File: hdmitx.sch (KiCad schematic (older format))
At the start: 56 parts, among them J4 HDMI_CONN, U15 TLV70018, U16 TLV70018, U3 IT6613, U8 PCM1862, Y2 24.576MHz

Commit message: add test pins fix tracks
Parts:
- added J21: I2C_BCK, custom_components:TestPad-D1.0mm, symbol Connector_Generic:Conn_01x01
- added J22: I2C_WS, custom_components:TestPad-D1.0mm, symbol Connector_Generic:Conn_01x01
- added J23: I2C_DATA, custom_components:TestPad-D1.0mm, symbol Connector_Generic:Conn_01x01
- added J24: I2C_MCLK, custom_components:TestPad-D1.0mm, symbol Connector_Generic:Conn_01x01
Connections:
- wire segments 132 -> 176
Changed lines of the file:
@@
 EESchema Schematic File Version 4
 LIBS:ossc_board-cache
-EELAYER 26 0
+EELAYER 30 0
 EELAYER END
 $Descr A4 11693 8268
@@
 $EndComp
 $Comp
-L ossc_board-rescue:GND-RESCUE-ossc_board #PWR0170
-U 1 1 5501F4D5
-P 2250 3000
-F 0 "#PWR0170" H 2250 3000 30  0001 C CNN
-F 1 "GND" H 2250 2930 30  0001 C CNN
-F 2 "" H 2250 3000 60  0001 C CNN
-F 3 "" H 2250 3000 60  0000 C CNN
-	1    2250 3000
-	0    1    1    0
-$EndComp
-$Comp
 L ossc_board-rescue:GND-RESCUE-ossc_board #PWR0171
 U 1 1 5501F4DB
@@
 AVCC1V8
 Wire Wire Line
-	3250 5500 3250 6500
+	3250 5500 3250 6450
 Wire Wire Line
 	3250 7200 3250 7650
@@
 	3000 7200 3000 6450
 Wire Wire Line
-	3000 6450 3250 6450
-Wire Wire Line
-	4650 5500 4650 6500
+	3000 6450 3100 6450
+Wire Wire Line
+	4650 5500 4650 6450
 Wire Wire Line
 	4650 7200 4650 7650
@@
 	4400 7200 4400 6450
 Wire Wire Line
-	4400 6450 4650 6450
-Wire Wire Line
-	3650 5500 3650 6500
+	4400 6450 4500 6450
+Wire Wire Line
+	3650 5500 3650 6450
 Wire Wire Line
 	3650 7200 3650 7650
@@
 	3400 7200 3400 6450
 Wire Wire Line
-	3400 6450 4250 6450
+	3400 6450 3500 6450
 Wire Wire Line
 	2700 6000 3150 6000
@@
 	6250 3700 6750 3700
 Wire Wire Line
-	5450 1900 5450 2100
-Wire Wire Line
-	3150 1900 3150 2100
-Wire Wire Line
 	1800 3700 2250 3700
 Wire Wire Line
@@
 	7500 5000 6250 5000
 Wire Wire Line
-	8500 2900 9450 2900
-Wire Wire Line
-	8500 3000 9450 3000
-Wire Wire Line
-	8500 3200 9450 3200
-Wire Wire Line
-	8500 3300 9450 3300
-Wire Wire Line
-	8500 3500 9450 3500
-Wire Wire Line
-	8500 3600 9450 3600
-Wire Wire Line
-	8500 3800 9450 3800
-Wire Wire Line
-	8500 3900 9450 3900
+	8500 2900 9100 2900
+Wire Wire Line
+	8500 3000 9100 3000
+Wire Wire Line
+	8500 3200 9100 3200
+Wire Wire Line
+	8500 3300 9100 3300
+Wire Wire Line
+	8500 3500 9100 3500
+Wire Wire Line
+	8500 3600 9100 3600
+Wire Wire Line
+	8500 3800 9100 3800
+Wire Wire Line
+	8500 3900 9100 3900
 Wire Wire Line
 	8050 6450 7600 6450
@@
 	9950 5900 9950 5950
 Wire Wire Line
-	9350 5950 10500 5950
-Wire Wire Line
-	10400 5550 10700 5550
+	9350 5950 9950 5950
+Wire Wire Line
+	10400 5550 10500 5550
 Wire Wire Line
 	9500 5550 9500 5700
@@
 	9950 6850 9950 6900
 Wire Wire Line
-	9350 6900 10500 6900
-Wire Wire Line
-	8750 6500 9500 6500
-Wire Wire Line
-	10400 6500 10700 6500
+	9350 6900 9950 6900
+Wire Wire Line
+	8750 6500 9350 6500
+Wire Wire Line
+	10400 6500 10500 6500
 Wire Wire Line
 	9500 6500 9500 6650
@@
 Wire Notes Line
 	10100 4600 10100 4500
-Wire Wire Line
-	3150 1600 3150 2000
-Connection ~ 3150 2000
-Wire Wire Line
-	5450 1950 5450 1600
-Connection ~ 5450 1950
 $Comp
 L ossc_board-rescue:FILTER FB4
@@
 Connection ~ 4000 6450
 Wire Wire Line
-	8750 5550 9500 5550
+	8750 5550 9350 5550
 Text Label 8850 5550 0    60   ~ 0
 DVDD3V3
@@
 DVDD1V8
 Wire Wire Line
-	8950 4650 9550 4650
+	8950 4650 9250 4650
 $Comp
 L ossc_board-rescue:R R41
@@
 DDC_SCL
 Wire Wire Line
-	8300 4250 9550 4250
-Wire Wire Line
-	7650 4350 9550 4350
+	8300 4250 8750 4250
+Wire Wire Line
+	7650 4350 8150 4350
 Text Label 7650 4350 0    60   ~ 0
 DDC_SDA
@@
 Connection ~ 8750 4250
 Wire Wire Line
-	8300 4550 9550 4550
+	8300 4550 8750 4550
 $Comp
 L ossc_board-rescue:PWR_FLAG #FLG0226
@@
 $EndComp
 Wire Wire Line
-	7700 2200 8250 2200
+	7700 2200 7900 2200
 Connection ~ 7900 2200
 $Comp
@@
 $EndComp
 Wire Wire Line
-	7250 1600 8250 1600
+	7250 1600 7450 1600
 Text Label 7300 1600 0    60   ~ 0
 AVCC3V3
@@
 	7650 1700 7650 1950
 Wire Wire Line
-	7650 1950 6900 1950
+	7650 1950 7100 1950
 Wire Wire Line
 	8250 1800 7750 1800
@@
 Wire Wire Line
 	2250 3400 1700 3400
-Wire Wire Line
-	2250 3500 1700 3500
-Wire Wire Line
-	2250 3600 1700 3600
 Text Label 1750 3400 0    60   ~ 0
 I2S_DATA
@@
 AV3_AUD_R
 Wire Wire Line
-	10050 900  10650 900
-Wire Wire Line
-	10050 1100 10650 1100
-Wire Wire Line
-	7250 900  8050 900
+	10050 900  10550 900
+Wire Wire Line
+	10050 1100 10450 1100
+Wire Wire Line
+	7250 900  7400 900
 Wire Wire Line
 	8750 4250 8750 4100
@@
 $EndComp
 Wire Wire Line
-	8500 3100 9400 3100
+	8500 3100 9100 3100
 Connection ~ 9100 3100
 Connection ~ 9400 3000
@@
 $EndComp
 Wire Wire Line
-	8500 3700 9400 3700
+	8500 3700 9100 3700
 Connection ~ 9100 3700
 Connection ~ 9400 3800
@@
 Connection ~ 7400 900
 Wire Wire Line
-	7250 1000 7800 1000
+	7250 1000 7400 1000
 Connection ~ 7400 1000
 $Comp
@@
 $EndComp
 Wire Wire Line
-	10200 1200 10650 1200
+	10200 1200 10550 1200
 $Comp
 L ossc_board-rescue:GND #PWR0246
@@
 $EndComp
 Wire Wire Line
-	10650 1000 10200 1000
+	10650 1000 10450 1000
 Wire Wire Line
 	10450 850  10450 1000
@@
 NoConn ~ 8250 1100
 NoConn ~ 8250 1200
+Wire Wire Line
+	3250 6450 3250 6500
+Wire Wire Line
+	4650 6450 4650 6500
+Wire Wire Line
+	3650 6450 3650 6500
+Wire Wire Line
+	3650 6450 4000 6450
+Wire Wire Line
+	9350 5550 9500 5550
+Wire Wire Line
+	10500 5550 10700 5550
+Wire Wire Line
+	9950 5950 10500 5950
+Wire Wire Line
+	9350 6500 9500 6500
+Wire Wire Line
+	10500 6500 10700 6500
+Wire Wire Line
+	9950 6900 10500 6900
+Wire Wire Line
+	3100 6450 3250 6450
+Wire Wire Line
+	3500 6450 3650 6450
+Wire Wire Line
+	4500 6450 4650 6450
+Wire Wire Line
+	4000 6450 4250 6450
+Wire Wire Line
+	9250 4650 9550 4650
+Wire Wire Line
+	8150 4350 9550 4350
+Wire Wire Line
+	8750 4250 9550 4250
+Wire Wire Line
+	8750 4550 9550 4550
+Wire Wire Line
+	7900 2200 8250 2200
+Wire Wire Line
+	7450 1600 8250 1600
+Wire Wire Line
+	7100 1950 6900 1950
+Wire Wire Line
+	9100 3100 9400 3100
+Wire Wire Line
+	9400 3000 9450 3000
+Wire Wire Line
+	9100 3000 9400 3000
+Wire Wire Line
+	9400 2900 9450 2900
+Wire Wire Line
+	9100 2900 9400 2900
+Wire Wire Line
+	9400 3200 9450 3200
+Wire Wire Line
+	9100 3200 9400 3200
+Wire Wire Line
+	9400 3300 9450 3300
+Wire Wire Line
+	9100 3300 9400 3300
+Wire Wire Line
+	9400 3500 9450 3500
+Wire Wire Line
+	9100 3500 9400 3500
+Wire Wire Line
+	9400 3600 9450 3600
+Wire Wire Line
+	9100 3600 9400 3600
+Wire Wire Line
+	9100 3700 9400 3700
+Wire Wire Line
+	9400 3800 9450 3800
+Wire Wire Line
+	9100 3800 9400 3800
+Wire Wire Line
+	9400 3900 9450 3900
+Wire Wire Line
+	9100 3900 9400 3900
+Wire Wire Line
+	7400 900  8050 900
+Wire Wire Line
+	7400 1000 7800 1000
+Wire Wire Line
+	10450 1000 10200 1000
+Wire Wire Line
+	10550 900  10650 900
+Wire Wire Line
+	10450 1100 10650 1100
+Wire Wire Line
+	10550 1200 10650 1200
+Wire Wire Line
+	3150 1600 3150 2100
+Wire Wire Line
+	5450 1600 5450 2100
+$Comp
+L Connector_Generic:Conn_01x01 J21
+U 1 1 5ED4EADB
+P 1200 3600
+F 0 "J21" H 1118 3375 50  0000 C CNN
+F 1 "I2C_BCK" H 1118 3466 50  0000 C CNN
+F 2 "custom_components:TestPad-D1.0mm" H 1200 3600 50  0001 C CNN
+F 3 "~" H 1200 3600 50  0001 C CNN
+	1    1200 3600
+	-1   0    0    1
+$EndComp
+$Comp
+L Connector_Generic:Conn_01x01 J22
+U 1 1 5ED547BE
+P 1350 3500
+F 0 "J22" H 1268 3275 50  0000 C CNN
+F 1 "I2C_WS" H 1268 3366 50  0000 C CNN
+F 2 "custom_components:TestPad-D1.0mm" H 1350 3500 50  0001 C CNN
+F 3 "~" H 1350 3500 50  0001 C CNN
+	1    1350 3500
+	-1   0    0    1
+$EndComp
+$Comp
+L Connector_Generic:Conn_01x01 J23
+U 1 1 5ED55109
+P 1500 3400
+F 0 "J23" H 1418 3175 50  0000 C CNN
+F 1 "I2C_DATA" H 1418 3266 50  0000 C CNN
+F 2 "custom_components:TestPad-D1.0mm" H 1500 3400 50  0001 C CNN
+F 3 "~" H 1500 3400 50  0001 C CNN
+	1    1500 3400
+	-1   0    0    1
+$EndComp
+Wire Wire Line
+	1550 3500 2250 3500
+Wire Wire Line
+	1400 3600 2250 3600
+$Comp
+L Connector_Generic:Conn_01x01 J24
+U 1 1 5ED68957
+P 1550 3000
+F 0 "J24" H 1468 2775 50  0000 C CNN
+F 1 "I2C_MCLK" H 1468 2866 50  0000 C CNN
+F 2 "custom_components:TestPad-D1.0mm" H 1550 3000 50  0001 C CNN
+F 3 "~" H 1550 3000 50  0001 C CNN
+	1    1550 3000
+	-1   0    0    1
+$EndComp
+Wire Wire Line
+	1750 3000 2250 3000
 $EndSCHEMATC

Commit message: remove unnecessary component
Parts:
- removed C111, C112: 30p, custom_components:SM0603_Capa_libcms, symbol ossc_board-rescue:C_Small
- removed C113, C115, C116, C121, C123, C124, C125, C126: 10u, custom_components:SM0603_Capa_libcms, symbol ossc_board-rescue:C_Small
- removed C114, C118: 0.1u, custom_components:SM0603_Capa_libcms, symbol ossc_board-rescue:C_Small
- removed C119, C120: 2.2u, custom_components:SM0603_Capa_libcms, symbol ossc_board-rescue:C_Small
- removed R47, R48, R49, R50, R51, R52: 100k, custom_components:SM0603_Resistor_libcms, symbol ossc_board-rescue:R_Small
- removed U8: PCM1862, custom_components:TSSOP-30_4.4x7.8mm_Pitch0.5mm_Handsoldering, symbol ossc_board-rescue:PCM1862
- removed Y2: 24.576MHz, custom_components:ECS-3X9X, symbol ossc_board-rescue:Crystal_Small
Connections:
- net labels removed: AV1_AUD_L, AV1_AUD_R, AV2_AUD_L, AV2_AUD_R, AV3_AUD_L, AV3_AUD_R
- wire segments 176 -> 129
- no-connect marks 10 -> 3

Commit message: update PCB
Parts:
- removed J21: I2C_BCK, custom_components:TestPad-D1.0mm, symbol Connector_Generic:Conn_01x01
- removed J22: I2C_WS, custom_components:TestPad-D1.0mm, symbol Connector_Generic:Conn_01x01
- removed J23: I2C_DATA, custom_components:TestPad-D1.0mm, symbol Connector_Generic:Conn_01x01
- removed J24: I2C_MCLK, custom_components:TestPad-D1.0mm, symbol Connector_Generic:Conn_01x01
- C110, C69, C73, C74, C75, C77, C78, C79, C80, C81, C82, C83, C84, C85, C86, C87, C88, C89, C90: footprint custom_components:SM0603_Capa_libcms -> Capacitor_SMD:C_0603_1608Metric_Pad1.05x0.95mm_HandSolder
- F1: renamed from F2; footprint custom_components:SM0603_Resistor_libcms -> Inductor_SMD:L_0603_1608Metric_Pad1.05x0.95mm_HandSolder
- FB1, FB2, FB4: footprint custom_components:SM0603_Resistor_libcms -> Inductor_SMD:L_0603_1608Metric_Pad1.05x0.95mm_HandSolder
- R25, R26, R41, R45, R46: footprint custom_components:SM0603_Resistor_libcms -> Resistor_SMD:R_0603_1608Metric_Pad1.05x0.95mm_HandSolder
- renumbered J4 to J1
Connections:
- net labels added: I2S_LRCK, I2S_MCLK
- net labels removed: I2S_WS

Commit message: update3
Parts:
- R25: value 698 -> 698 1%
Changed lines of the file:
@@
 P 3150 5750
 F 0 "R25" V 3230 5750 40  0000 C CNN
-F 1 "698" V 3157 5751 40  0000 C CNN
+F 1 "698 1%" V 3157 5751 40  0000 C CNN
 F 2 "Resistor_SMD:R_0603_1608Metric_Pad1.05x0.95mm_HandSolder" V 3080 5750 30  0001 C CNN
 F 3 "~" H 3150 5750 30  0000 C CNN

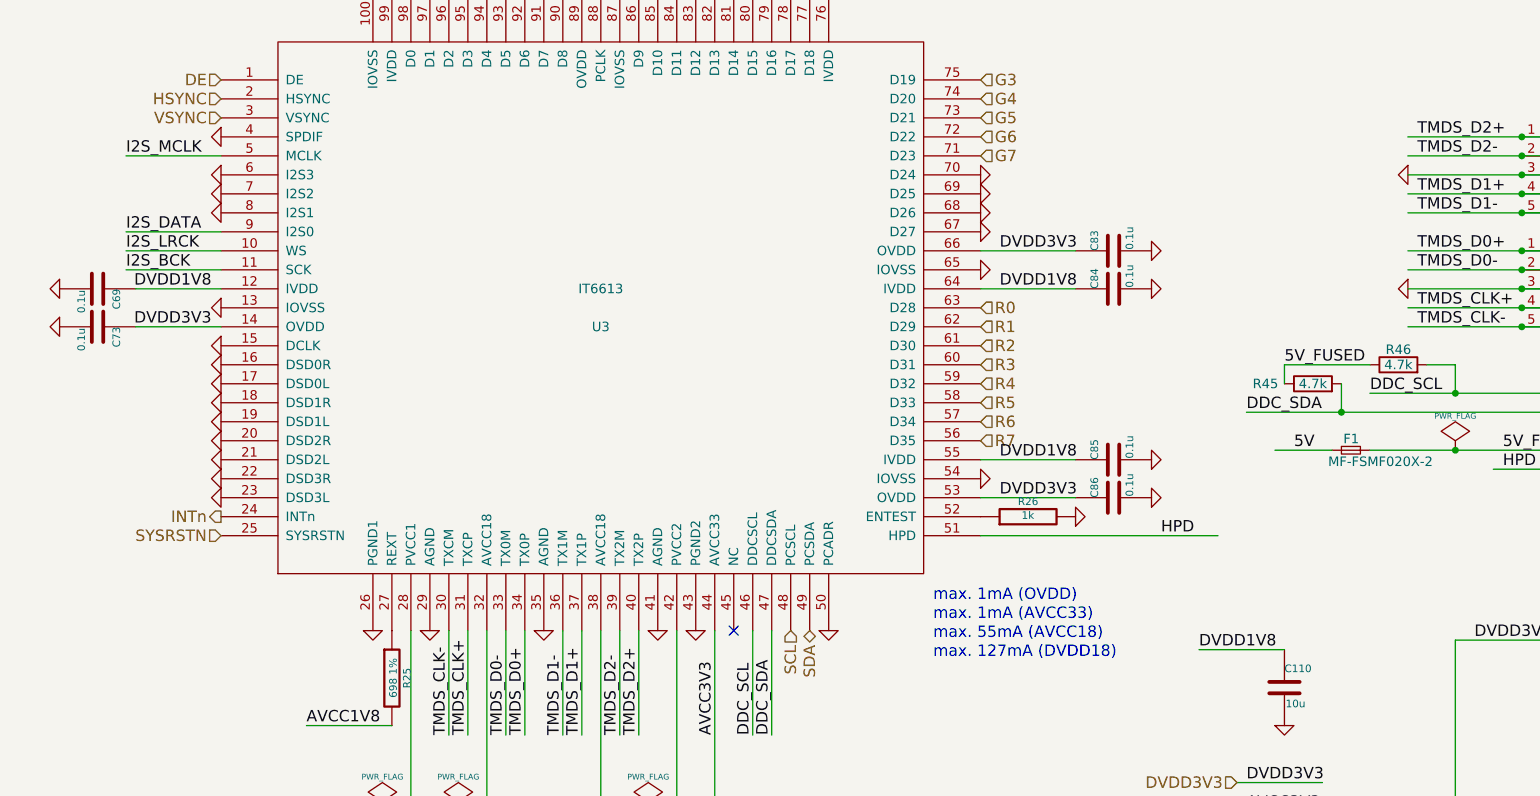
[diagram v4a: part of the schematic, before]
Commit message: add adc
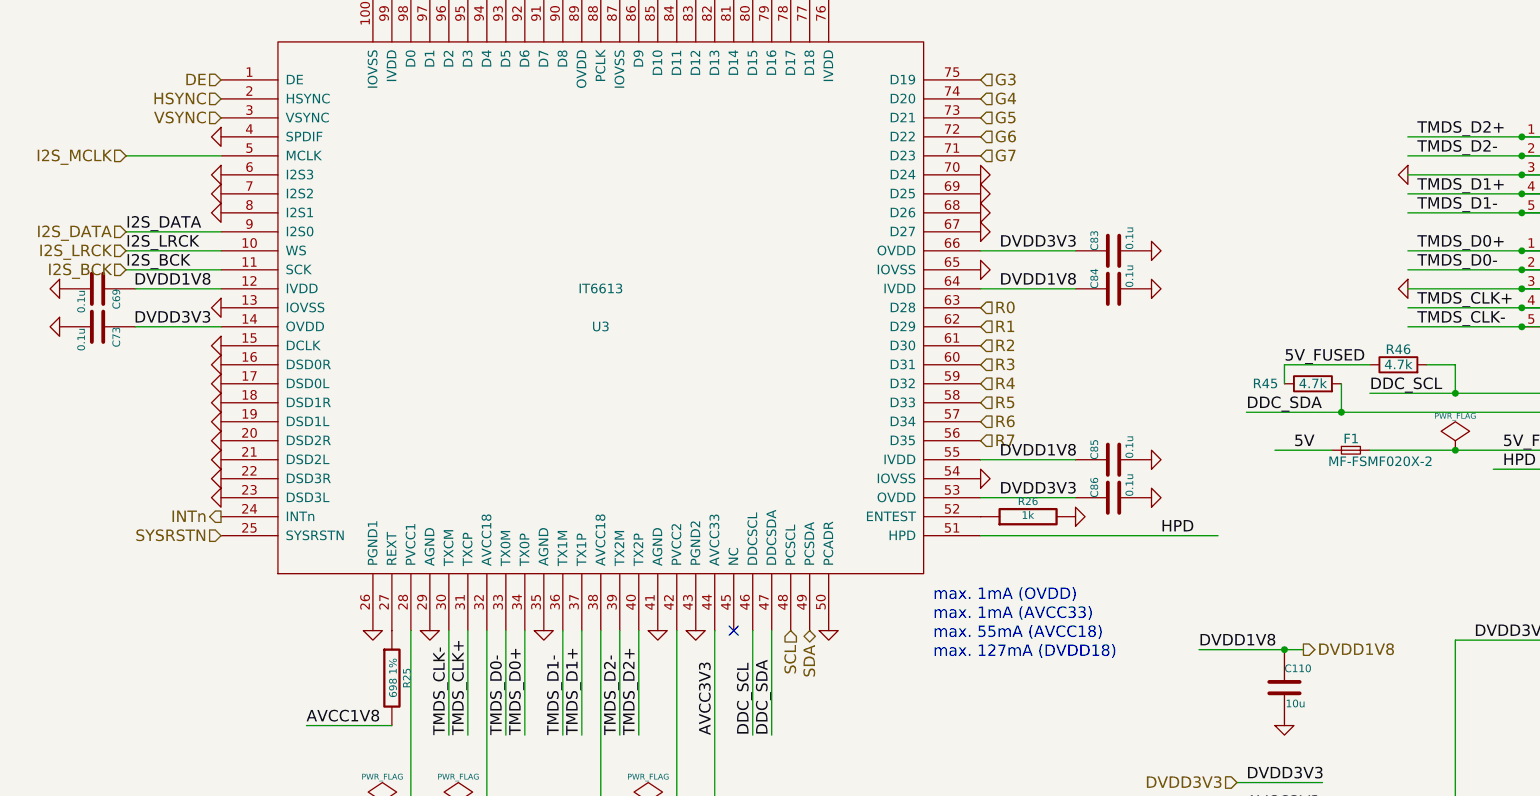
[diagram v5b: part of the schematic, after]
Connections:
- wire segments 129 -> 130
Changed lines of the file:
@@
 Text Label 7850 4100 0    60   ~ 0
 5V_FUSED
-Text Label 1750 3400 0    60   ~ 0
-I2S_DATA
 Text Label 1750 3600 0    60   ~ 0
 I2S_BCK
@@
 Wire Wire Line
 	1750 3000 2250 3000
-Text Label 1750 3000 0    60   ~ 0
+Wire Wire Line
+	2250 3600 1750 3600
+Wire Wire Line
+	1750 3500 2250 3500
+Wire Wire Line
+	2250 3400 1750 3400
+Text HLabel 7950 5600 2    60   Output ~ 0
+DVDD1V8
+Wire Wire Line
+	7950 5600 7850 5600
+Connection ~ 7850 5600
+Text HLabel 1750 3000 0    60   Input ~ 0
 I2S_MCLK
-Wire Wire Line
-	2250 3600 1750 3600
-Wire Wire Line
-	1750 3500 2250 3500
-Wire Wire Line
-	2250 3400 1750 3400
+Text Label 1750 3400 0    60   ~ 0
+I2S_DATA
+Text HLabel 1750 3400 0    60   Input ~ 0
+I2S_DATA
+Text HLabel 1750 3500 0    60   Input ~ 0
+I2S_LRCK
+Text HLabel 1750 3600 0    60   Input ~ 0
+I2S_BCK
 $EndSCHEMATC

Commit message: update PCB
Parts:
- J1: value HDMI_CONN -> HDMI_CONN (10029449-111RLF)
- U3: value IT6613 -> IT6613E
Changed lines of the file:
@@
 P 4250 3800
 F 0 "U3" H 4250 3700 50  0000 C CNN
-F 1 "IT6613" H 4250 3900 50  0000 C CNN
+F 1 "IT6613E" H 4250 3900 50  0000 C CNN
 F 2 "custom_components:TQFP-100_custom" H 4250 3800 50  0001 C CNN
 F 3 "DOCUMENTATION" H 4250 3800 50  0001 C CNN
@@
 P 10300 3750
 F 0 "J1" H 10550 3350 50  0000 C CNN
-F 1 "HDMI_CONN" V 10650 3750 50  0000 C CNN
+F 1 "HDMI_CONN (10029449-111RLF)" V 10650 3750 50  0000 C CNN
 F 2 "custom_components:HDMI_CONN-10029449-111RLF" H 10300 3750 50  0001 C CNN
 F 3 "DOCUMENTATION" H 10300 3750 50  0001 C CNN

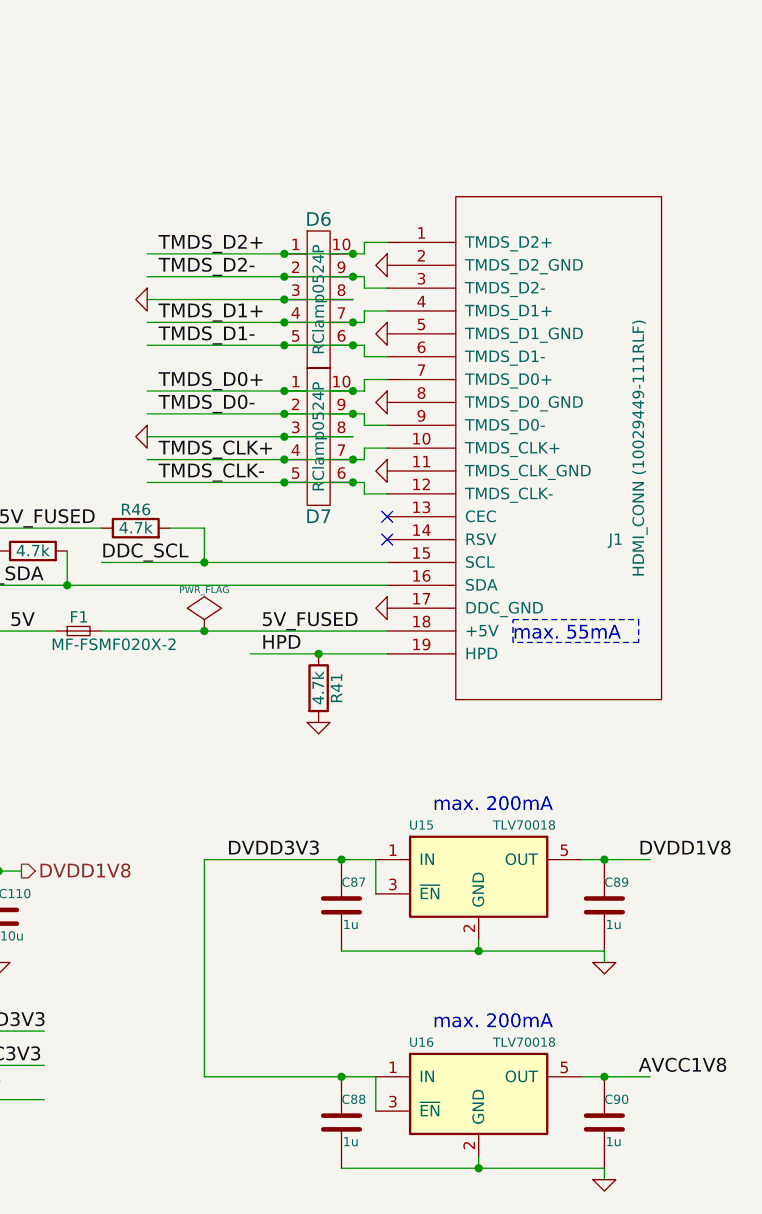
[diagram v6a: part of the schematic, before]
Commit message: update part no
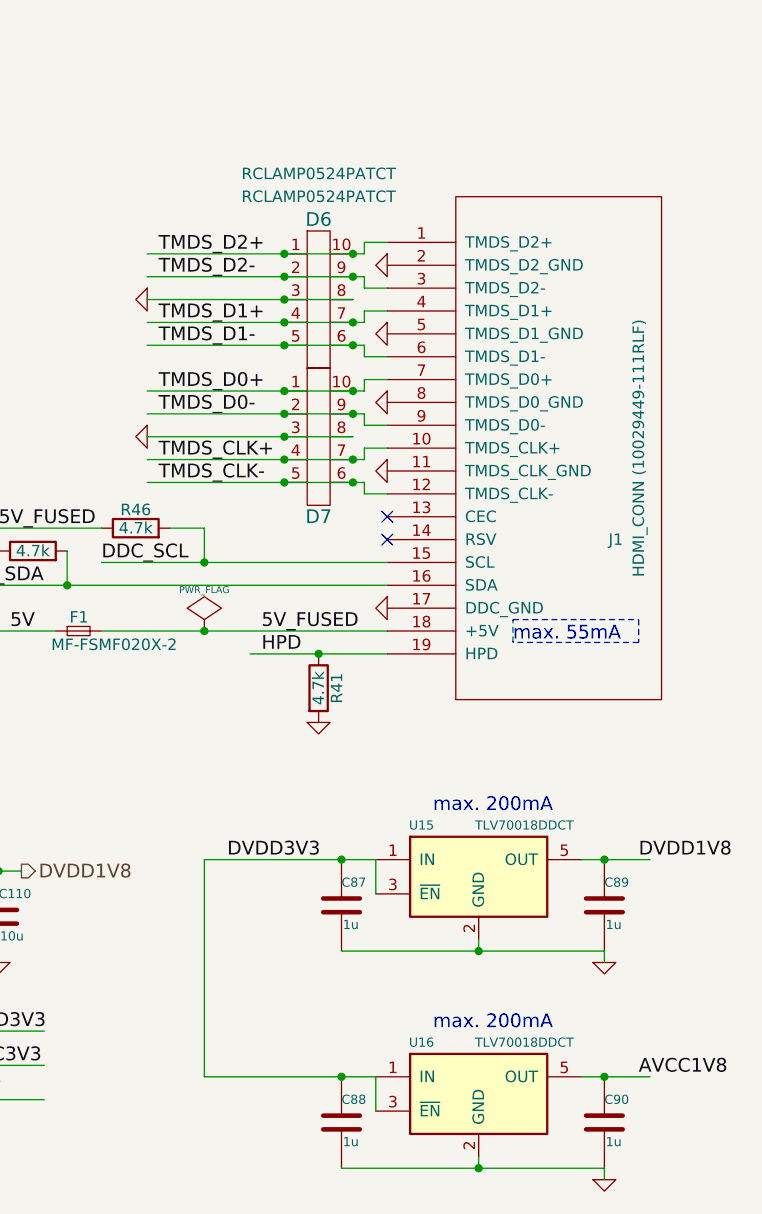
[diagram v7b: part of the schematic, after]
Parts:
- D6, D7: value RClamp0524P -> RCLAMP0524PATCT
- U15, U16: value TLV70018 -> TLV70018DDCT
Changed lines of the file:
@@
 AR Path="/54FF6758/5502F816" Ref="U15"  Part="1"
 F 0 "U15" H 9700 5800 40  0000 C CNN
-F 1 "TLV70018" H 10150 5800 40  0000 C CNN
+F 1 "TLV70018DDCT" H 10150 5800 40  0000 C CNN
 F 2 "custom_components:SOT-23-5_Handsoldering" H 9950 5700 35  0001 C CIN
 F 3 "" H 9950 5600 60  0000 C CNN
@@
 AR Path="/54FF6758/5502F844" Ref="U16"  Part="1"
 F 0 "U16" H 9700 6750 40  0000 C CNN
-F 1 "TLV70018" H 10150 6750 40  0000 C CNN
+F 1 "TLV70018DDCT" H 10150 6750 40  0000 C CNN
 F 2 "custom_components:SOT-23-5_Handsoldering" H 9950 6650 35  0001 C CIN
 F 3 "" H 9950 6550 60  0000 C CNN
@@
 P 9250 3100
 F 0 "D6" H 9250 3450 60  0000 C CNN
-F 1 "RClamp0524P" V 9250 3100 50  0000 C CNN
+F 1 "RCLAMP0524PATCT" H 9250 3550 50  0000 C CNN
 F 2 "custom_components:SLP2510P8" H 9300 3150 60  0001 C CNN
 F 3 "" H 9300 3150 60  0001 C CNN
@@
 P 9250 3700
 F 0 "D7" H 9250 3350 60  0000 C CNN
-F 1 "RClamp0524P" V 9250 3700 50  0000 C CNN
+F 1 "RCLAMP0524PATCT" H 9250 4850 50  0000 C CNN
 F 2 "custom_components:SLP2510P8" H 9300 3750 60  0001 C CNN
 F 3 "" H 9300 3750 60  0001 C CNN
